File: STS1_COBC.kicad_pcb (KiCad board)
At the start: 4 copper layers, 81 x 85 mm, 207 parts, among them J1 UHF, J16 SWD, Q1 SQ2318, Q2 BSS123, Q3 SQ2318, Q4 SQ2318, U1 W25Q01JVZEIQ, U10 TQP3M9036, U11 NL17SV04XV5T2G, U12 FPF2701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

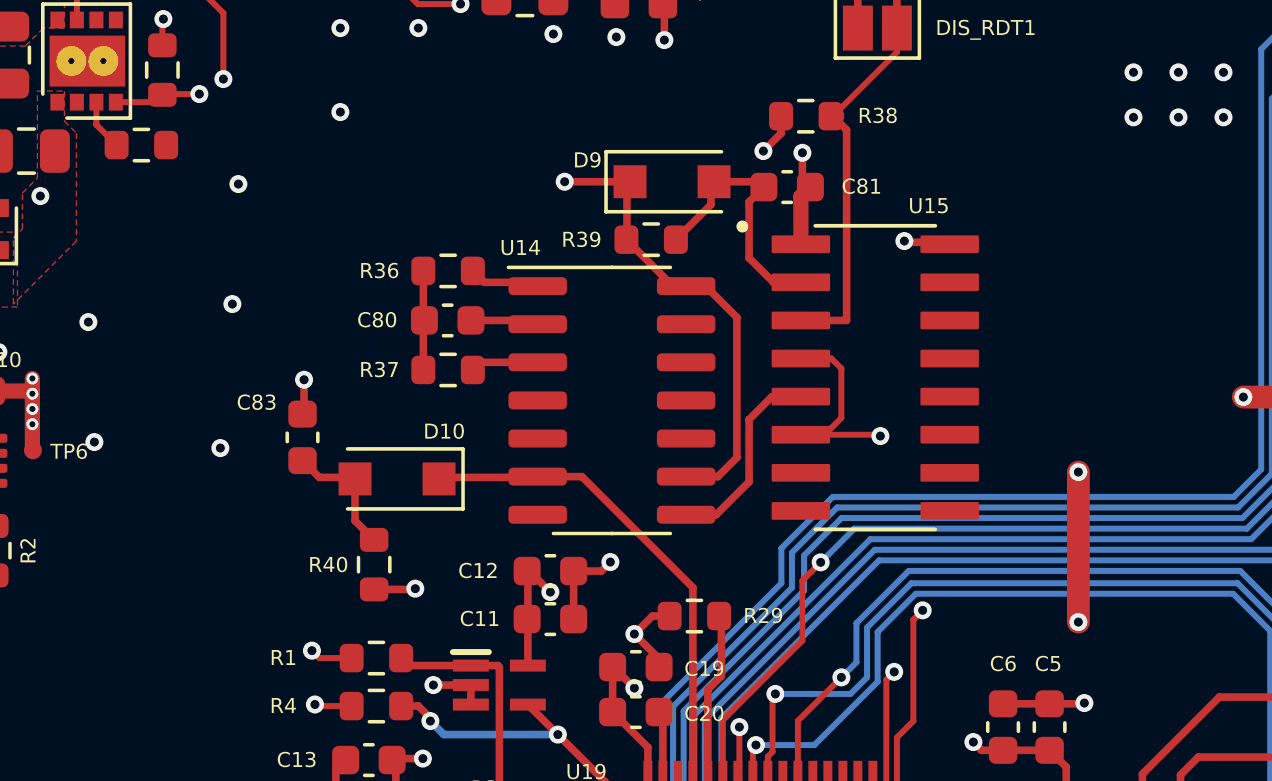
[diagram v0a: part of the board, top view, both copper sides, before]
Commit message: Make changes to the RDT: switch off AR, add Schmidt trigger for MR, change values of R40 and C83
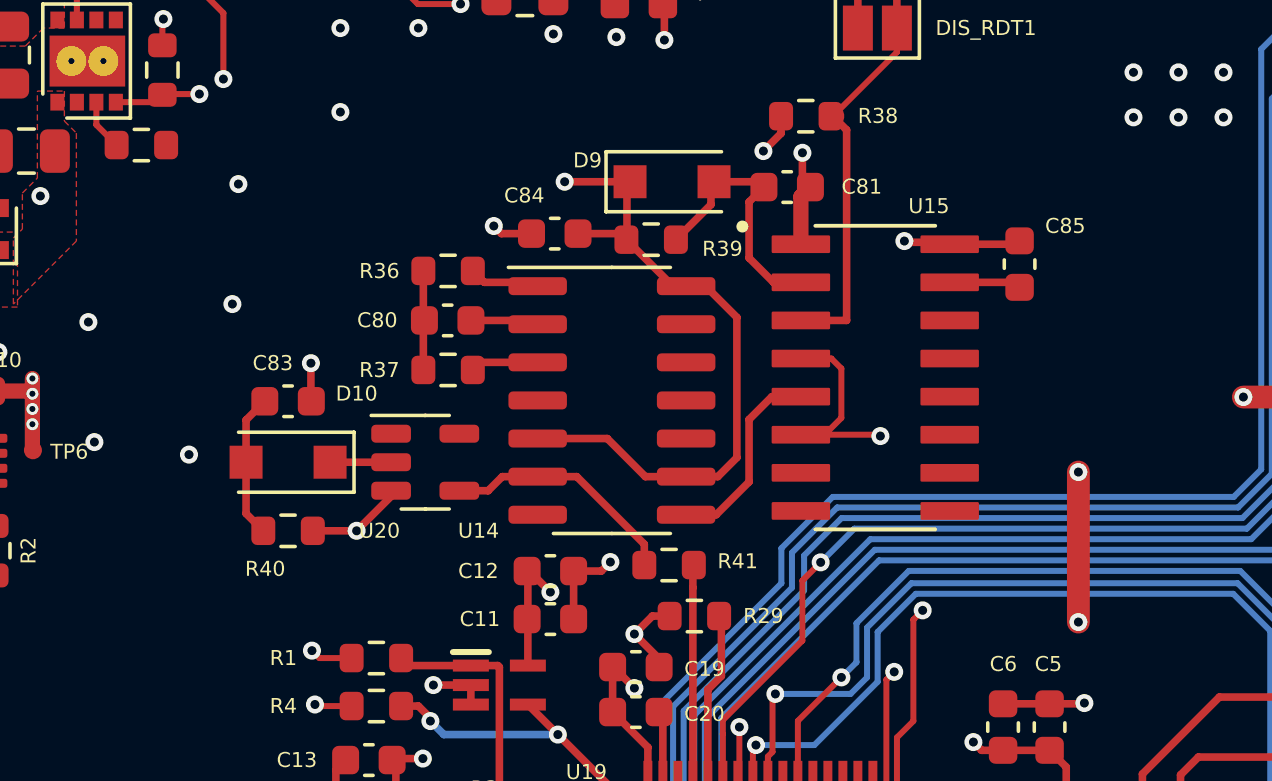
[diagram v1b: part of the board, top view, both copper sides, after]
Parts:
- added C84: 100n, Capacitor_SMD:C_0603_1608Metric, F.Cu at (165.5, 77.1)
- added C85: 100n, Capacitor_SMD:C_0603_1608Metric, F.Cu at (181.0, 78.1)
- added R41: 100, Resistor_SMD:R_0603_1608Metric, F.Cu at (169.4, 88.1)
- added U20: 74LVC1G17, Package_TO_SOT_SMD:SOT-23-5, F.Cu at (161.2, 84.7)
- C83: value 1n -> 10u
- R40: value 10K -> 22k
- moved D10 3.67 mm to (156.7, 84.7)
- moved R40 3.08 mm to (156.7, 87.0), turned to 0 degrees
- moved C83 1.30 mm to (156.7, 82.6), turned to 180 degrees
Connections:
- D10 pad 1: /RDT_Clear -> Net-(D10-Pad1)
- U14 pad 5: GND -> +3V3
- U14 pad 6: /RDT_Clear -> Net-(U14-Pad6)
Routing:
- net +3V3: track 121.9 -> 131.6 mm
- net /RDT_Clear: track 16.4 -> 7.27 mm
- net Net-(U14-Pad6): track 0.00 -> 7.99 mm
- net GND: track 199.8 -> 205.5 mm, vias 514 -> 515
- net Net-(D10-Pad1): track 0.00 -> 2.03 mm

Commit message: Change version to 2.7
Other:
- board text added: "TU Wien Space Team STS1 COBC V2.7"
- board text removed: "TU Wien Space Team STS1 COBC V3.0"
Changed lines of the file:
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@@
     (property "Sheetname" "Resetdog")
     (attr smd)
-    (fp_text reference "D10" (at -2.286 2.286) (layer "F.SilkS")
+    (fp_text reference "D10" (at 3.048 -0.762) (layer "F.SilkS")
       (effects (font (size 0.5 0.5) (thickness 0.1)))
     )
@@
     (property "Sheetname" "Resetdog")
     (attr smd)
-    (fp_text reference "U20" (at -1.524 2.286) (layer "F.SilkS")
+    (fp_text reference "U20" (at 0 2.286) (layer "F.SilkS")
       (effects (font (size 0.5 0.5) (thickness 0.1)))
     )
@@
   (gr_line (start 115 46.5) (end 115 122.5) (layer "Edge.Cuts") (width 0.15))
   (gr_line (start 180 127) (end 191.5 127) (layer "Edge.Cuts") (width 0.15))
-  (gr_text "TU Wien Space Team STS1\nCOBC\nV3.0" (at 149.2 120.8) (layer "F.SilkS")
+  (gr_text "TU Wien Space Team STS1\nCOBC\nV2.7" (at 149.2 120.8) (layer "F.SilkS")
     (effects (font (size 1.2 1.2) (thickness 0.2)))
   )
